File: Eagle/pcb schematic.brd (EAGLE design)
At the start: 100 x 80 mm, 17 parts

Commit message: PCB finita
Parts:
- BLUETOOTH: device SparkFun-Connectors:1X02 -> SparkFun-Connectors:1X04
- moved R5 24.3 mm to (34.3, 39.4), turned to 0 degrees
- moved R6 16.1 mm to (50.8, 40.6), turned to 0 degrees
- moved R1 16.1 mm to (27.9, 30.5), turned to 90 degrees
- moved R7 12.8 mm to (61.0, 38.1), turned to 180 degrees
- moved FLEX1 12.7 mm to (30.5, 47.0), turned to 270 degrees
- moved FLEX2 11.4 mm to (47.0, 47.0), turned to 270 degrees
- moved BLUETOOTH 10.5 mm to (41.9, 30.5), turned to 0 degrees
- moved FSR 10.2 mm to (71.1, 47.0)
- moved FLEX3 10.2 mm to (61.0, 47.0)
- moved PIN_10 8.89 mm to (41.9, 25.4)
- moved R8 7.18 mm to (74.9, 35.6)
- moved J1 6.35 mm to (19.1, 44.5), turned to 90 degrees
- moved D1 5.24 mm to (34.3, 29.2)
- moved PIN_123-124 5.08 mm to (54.6, 25.4), turned to 180 degrees
- moved PIN_26-24 3.81 mm to (74.9, 25.4)
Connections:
- net GND: now also BLUETOOTH.2
- net N$4: now also BLUETOOTH.4, PIN_123-124.1; no longer BLUETOOTH.1, PIN_123-124.2
- net N$6: now also BLUETOOTH.3, PIN_123-124.2; no longer BLUETOOTH.2, PIN_123-124.1
- net N$9: now also BLUETOOTH.1
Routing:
- net N$9: track 0.00 -> 88.4 mm
- net N$1: track 0.00 -> 47.7 mm
- net N$2: track 0.00 -> 33.0 mm
- net N$3: track 0.00 -> 26.0 mm
- net N$5: track 0.00 -> 22.1 mm
- net N$4: track 0.00 -> 10.2 mm
- net N$10: track 0.00 -> 8.83 mm
- net N$11: track 0.00 -> 8.09 mm
- net N$6: track 0.00 -> 7.18 mm
- net 5V: track 0.00 -> 5.74 mm
- added copper zone on layer 1, net GND

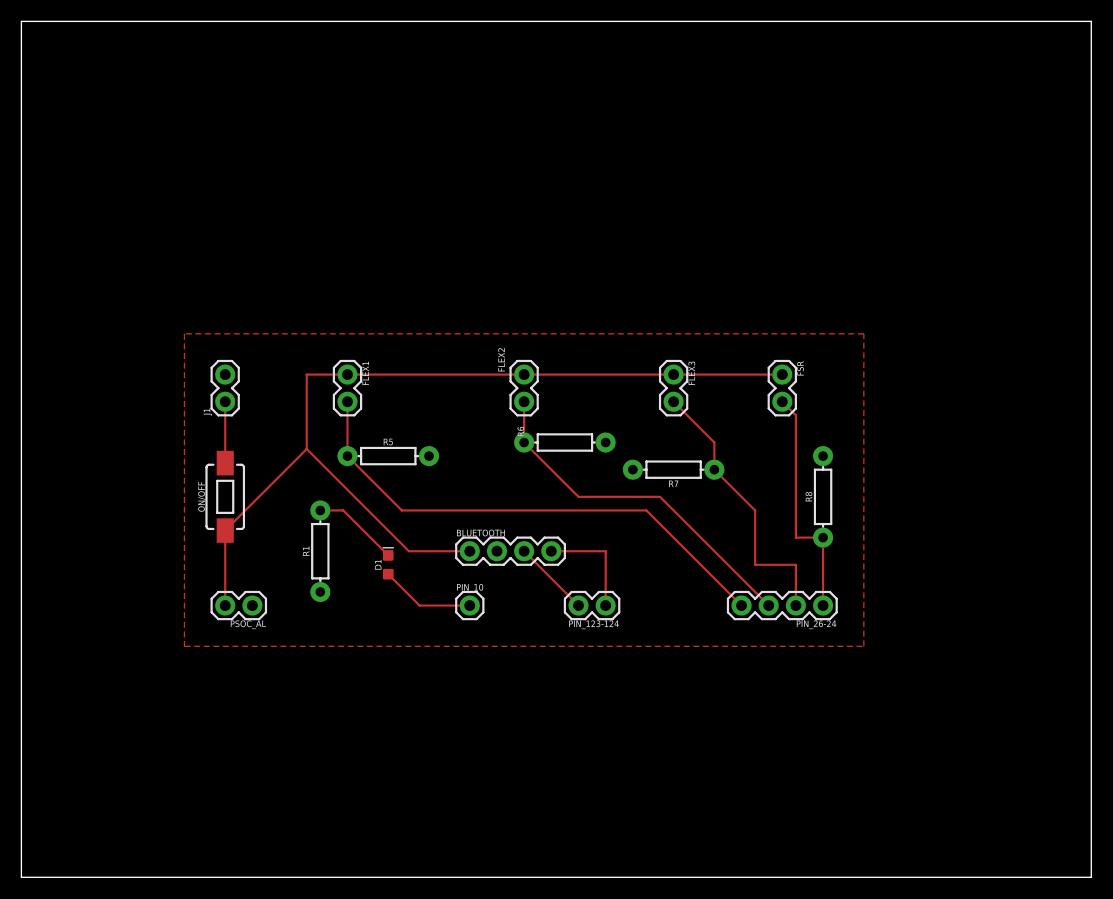
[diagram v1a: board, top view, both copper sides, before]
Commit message: PCB modifica tracce e aggiunta componenti batteria
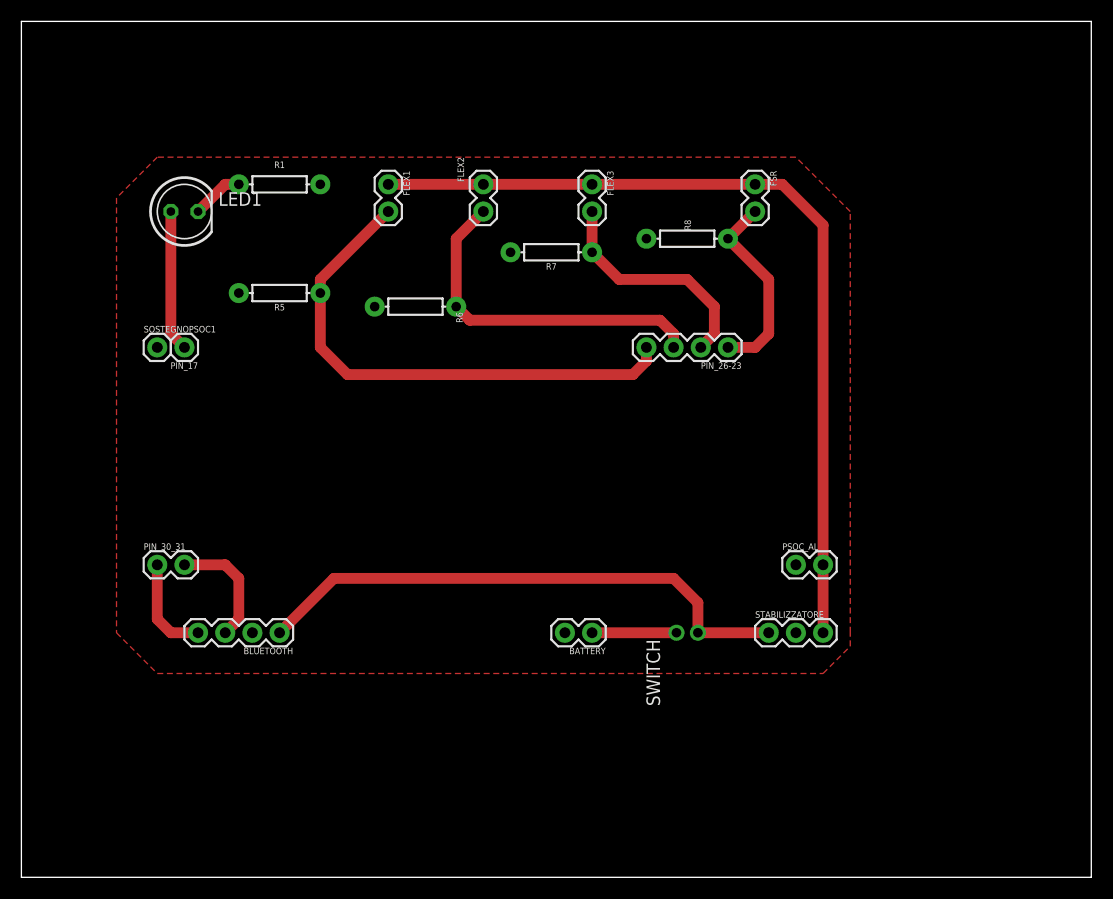
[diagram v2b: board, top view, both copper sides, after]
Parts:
- removed D1: RED, SparkFun-LED:LED-0603
- removed J1, PIN_123-124: (no value), SparkFun-Connectors:1X02
- removed ON/OFF: MOMENTARY-SWITCH-SPST-SMD-6.0X3.5MM, SparkFun-Switches:TACTILE_SWITCH_SMD_6.0X3.5MM
- removed PIN_10: (no value), SparkFun-Connectors:1X01
- removed PIN_26-24: (no value), SparkFun-Connectors:1X04
- added BATTERY, PIN_30_31: (no value), SparkFun-Connectors:1X02
- added LED1: (no value), led:LED5MM
- added PIN_17, SOSTEGNOPSOC1: (no value), SparkFun-Connectors:1X01
- added PIN_26-23: (no value), SparkFun-Connectors:1X04
- added STABILIZZATORE: 455-1750-1-ND, SparkFun-Connectors:1X03
- added SWITCH: 332-02, con-garry:332-02
- moved PSOC_AL 50.9 mm to (72.4, 29.2), turned to 0 degrees
- moved R1 34.5 mm to (24.1, 64.8), turned to 180 degrees
- moved R8 27.3 mm to (62.2, 59.7), turned to 180 degrees
- moved R7 23.3 mm to (49.5, 58.4)
- moved BLUETOOTH 19.3 mm to (24.1, 22.9), turned to 180 degrees
- moved FLEX3 19.3 mm to (53.3, 64.8)
- moved R6 18.9 mm to (36.8, 53.3), turned to 180 degrees
- moved R5 18.3 mm to (24.1, 54.6), turned to 180 degrees
- moved FLEX1 18.2 mm to (34.3, 64.8)
- moved FLEX2 18.2 mm to (43.2, 64.8)
- moved FSR 18.0 mm to (68.6, 64.8)
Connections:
- removed net N$11: D1.C, R1.P$2
- removed net N$9: BLUETOOTH.1, FLEX1.1, FLEX2.1, FLEX3.1, FSR.1, ON/OFF.1, PSOC_AL.2
- new net N$12: FLEX1.1, FLEX2.1, FLEX3.1, FSR.1, PSOC_AL.2, STABILIZZATORE.3
- new net N$7: LED1.A, PIN_17.1
- new net N$8: LED1.K, R1.P$2
- net 5V: now also BATTERY.1, SWITCH.1; no longer J1.1, ON/OFF.2
- net GND: now also BATTERY.2, STABILIZZATORE.2; no longer J1.2
- net N$1: now also PIN_26-23.4; no longer PIN_26-24.4
- net N$10: now also BLUETOOTH.1, STABILIZZATORE.1, SWITCH.2; no longer D1.A, PIN_10.1
- net N$2: now also PIN_26-23.3; no longer PIN_26-24.3
- net N$3: now also PIN_26-23.2; no longer PIN_26-24.2
- net N$4: now also BLUETOOTH.3, PIN_30_31.2; no longer BLUETOOTH.4, PIN_123-124.1
- net N$5: now also PIN_26-23.1; no longer PIN_26-24.1
- net N$6: now also BLUETOOTH.4, PIN_30_31.1; no longer BLUETOOTH.3, PIN_123-124.2
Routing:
- net N$9: track 88.4 -> 0.00 mm
- net N$12: track 0.00 -> 80.3 mm
- net N$10: track 8.83 -> 51.6 mm
- net N$7: track 0.00 -> 13.2 mm
- net N$11: track 8.09 -> 0.00 mm
- net N$8: track 0.00 -> 4.86 mm
- net N$3: track 26.0 -> 21.7 mm
- net N$5: track 22.1 -> 18.4 mm
- net N$6: track 7.18 -> 9.42 mm
- net 5V: track 5.74 -> 7.89 mm
- net N$4: track 10.2 -> 11.2 mm
- net N$1: track 47.7 -> 48.7 mm

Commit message: PCB con pin separati senza errori
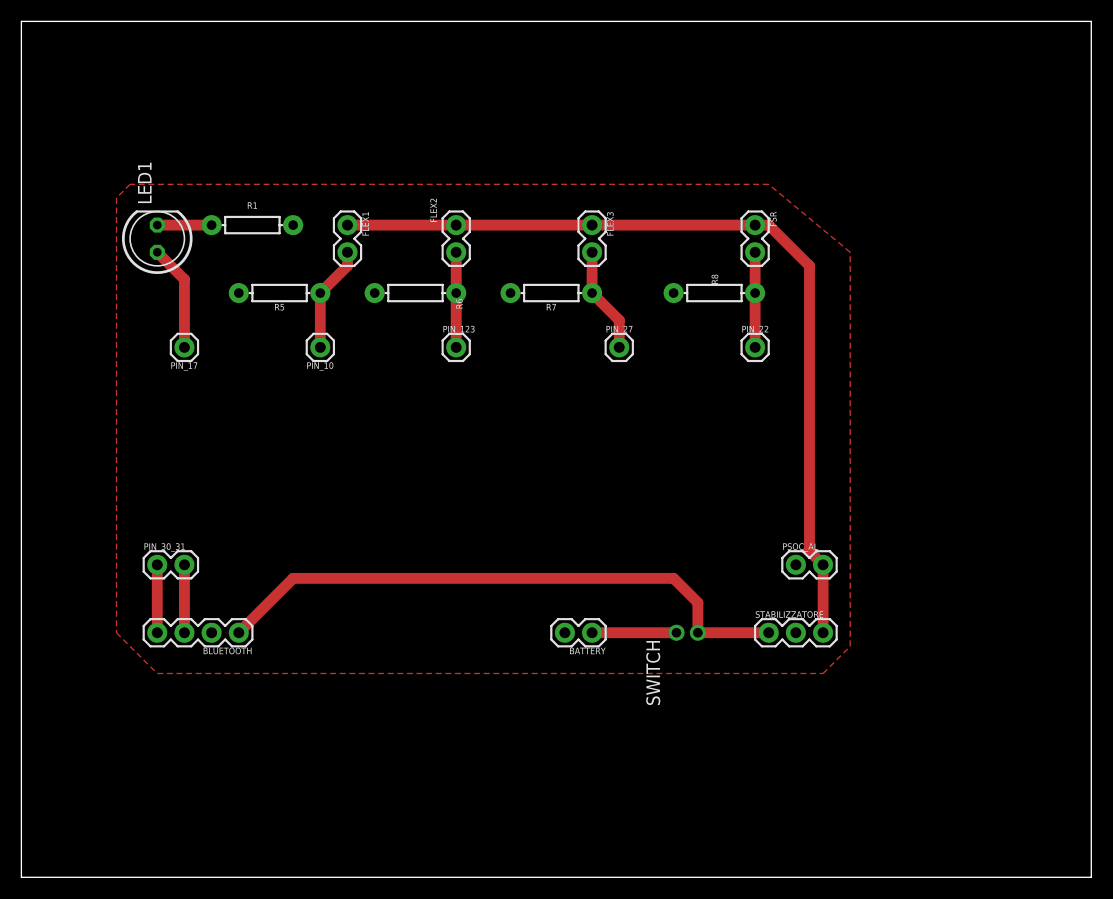
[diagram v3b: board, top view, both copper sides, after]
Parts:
- removed PIN_26-23: (no value), SparkFun-Connectors:1X04
- removed SOSTEGNOPSOC1: (no value), SparkFun-Connectors:1X01
- added PIN_10, PIN_123, PIN_22, PIN_27: (no value), SparkFun-Connectors:1X01
- moved R8 5.68 mm to (64.8, 54.6)
- moved FLEX1 5.39 mm to (30.5, 61.0)
- moved FLEX2 4.58 mm to (40.6, 61.0)
- moved R1 4.58 mm to (21.6, 61.0)
- moved R7 3.81 mm to (49.5, 54.6)
- moved BLUETOOTH 3.81 mm to (20.3, 22.9)
- moved FLEX3 3.81 mm to (53.3, 61.0)
- moved FSR 3.81 mm to (68.6, 61.0)
- moved LED1 3.59 mm to (12.7, 59.7), turned to 90 degrees
- moved R6 1.27 mm to (36.8, 54.6)
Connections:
- net N$1: now also PIN_10.1; no longer PIN_26-23.4
- net N$2: now also PIN_123.1; no longer PIN_26-23.3
- net N$3: now also PIN_27.1; no longer PIN_26-23.2
- net N$5: now also PIN_22.1; no longer PIN_26-23.1
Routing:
- net N$1: track 48.7 -> 9.94 mm
- net N$2: track 32.6 -> 8.89 mm
- net N$3: track 21.7 -> 9.94 mm
- net N$5: track 18.4 -> 8.89 mm
- net N$4: track 11.2 -> 6.35 mm
- net N$10: track 51.6 -> 55.4 mm
- net N$7: track 13.2 -> 9.94 mm
- net N$6: track 9.42 -> 6.35 mm
- net N$12: track 80.3 -> 79.6 mm

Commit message: PCB con pin separati senza errori
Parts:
- removed PIN_10, PIN_123: (no value), SparkFun-Connectors:1X01
- added PIN_12, PIN_25: (no value), SparkFun-Connectors:1X01
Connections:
- net N$1: now also PIN_12.1; no longer PIN_10.1
- net N$2: now also PIN_27.1; no longer PIN_123.1
- net N$3: now also PIN_25.1; no longer PIN_27.1
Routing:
- net N$2: track 8.89 -> 21.2 mm
- net N$3: track 9.94 -> 15.0 mm
- net N$1: track 9.94 -> 12.0 mm
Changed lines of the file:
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@@
 <attribute name="VALUE" x="68.58" y="20.828" size="0.6096" layer="27" font="vector" ratio="20"/>
 </element>
-<element name="PIN_10" library="SparkFun-Connectors" package="1X01" value="" x="27.94" y="49.53" smashed="yes" rot="R180">
-<attribute name="NAME" x="29.21" y="48.133" size="0.6096" layer="25" font="vector" ratio="20" rot="R180"/>
-<attribute name="VALUE" x="29.21" y="51.054" size="0.6096" layer="27" font="vector" ratio="20" rot="R180" align="top-left"/>
-</element>
-<element name="PIN_123" library="SparkFun-Connectors" package="1X01" value="" x="40.64" y="49.53" smashed="yes">
-<attribute name="NAME" x="39.37" y="50.927" size="0.6096" layer="25" font="vector" ratio="20"/>
-<attribute name="VALUE" x="39.37" y="48.006" size="0.6096" layer="27" font="vector" ratio="20" align="top-left"/>
+<element name="PIN_12" library="SparkFun-Connectors" package="1X01" value="" x="22.86" y="49.53" smashed="yes" rot="R180">
+<attribute name="NAME" x="24.13" y="48.133" size="0.6096" layer="25" font="vector" ratio="20" rot="R180"/>
+<attribute name="VALUE" x="24.13" y="51.054" size="0.6096" layer="27" font="vector" ratio="20" rot="R180" align="top-left"/>
 </element>
 <element name="PIN_27" library="SparkFun-Connectors" package="1X01" value="" x="55.88" y="49.53" smashed="yes">
 <attribute name="NAME" x="54.61" y="50.927" size="0.6096" layer="25" font="vector" ratio="20"/>
 <attribute name="VALUE" x="54.61" y="48.006" size="0.6096" layer="27" font="vector" ratio="20" align="top-left"/>
+</element>
+<element name="PIN_25" library="SparkFun-Connectors" package="1X01" value="" x="60.96" y="49.53" smashed="yes">
+<attribute name="NAME" x="59.69" y="50.927" size="0.6096" layer="25" font="vector" ratio="20"/>
+<attribute name="VALUE" x="59.69" y="48.006" size="0.6096" layer="27" font="vector" ratio="20" align="top-left"/>
 </element>
 <element name="PIN_22" library="SparkFun-Connectors" package="1X01" value="" x="68.58" y="49.53" smashed="yes">
@@
 <contactref element="R6" pad="P$1"/>
 <wire x1="40.64" y1="58.42" x2="40.64" y2="54.61" width="1.016" layer="1"/>
-<contactref element="PIN_123" pad="1"/>
-<wire x1="40.64" y1="54.61" x2="40.64" y2="49.53" width="1.016" layer="1"/>
+<contactref element="PIN_27" pad="1"/>
+<wire x1="55.88" y1="49.53" x2="45.72" y2="49.53" width="1.016" layer="1"/>
+<wire x1="40.64" y1="54.61" x2="45.72" y2="49.53" width="1.016" layer="1"/>
 </signal>
 <signal name="N$3">
@@
 <contactref element="R7" pad="P$1"/>
 <wire x1="53.34" y1="58.42" x2="53.34" y2="54.61" width="1.016" layer="1"/>
-<contactref element="PIN_27" pad="1"/>
-<wire x1="53.34" y1="54.61" x2="55.88" y2="52.07" width="1.016" layer="1"/>
-<wire x1="55.88" y1="52.07" x2="55.88" y2="49.53" width="1.016" layer="1"/>
+<contactref element="PIN_25" pad="1"/>
+<wire x1="53.34" y1="54.61" x2="58.42" y2="54.61" width="1.016" layer="1"/>
+<wire x1="58.42" y1="54.61" x2="60.96" y2="52.07" width="1.016" layer="1"/>
+<wire x1="60.96" y1="52.07" x2="60.96" y2="49.53" width="1.016" layer="1"/>
 </signal>
 <signal name="N$1">
@@
 <wire x1="30.48" y1="58.42" x2="30.48" y2="57.15" width="1.016" layer="1"/>
 <wire x1="30.48" y1="57.15" x2="27.94" y2="54.61" width="1.016" layer="1"/>
-<contactref element="PIN_10" pad="1"/>
-<wire x1="27.94" y1="54.61" x2="27.94" y2="49.53" width="1.016" layer="1"/>
+<contactref element="PIN_12" pad="1"/>
+<wire x1="27.94" y1="54.61" x2="22.86" y2="49.53" width="1.016" layer="1"/>
 </signal>
 <signal name="5V">

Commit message: case finito + modifica pcb
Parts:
- removed PIN_30_31: (no value), SparkFun-Connectors:1X02
- added PIN_35_36: (no value), SparkFun-Connectors:1X02
- moved BLUETOOTH 12.7 mm to (33.0, 22.9)
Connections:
- net N$4: now also PIN_35_36.2; no longer PIN_30_31.2
- net N$6: now also PIN_35_36.1; no longer PIN_30_31.1
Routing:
- net N$10: track 55.4 -> 42.7 mm
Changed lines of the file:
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@@
 <attribute name="VALUE" x="23.114" y="59.69" size="0.6096" layer="27" font="vector" ratio="20" align="top-center"/>
 </element>
-<element name="PIN_30_31" library="SparkFun-Connectors" package="1X02" value="" x="12.7" y="29.21" smashed="yes">
-<attribute name="NAME" x="11.43" y="30.607" size="0.6096" layer="25" font="vector" ratio="20"/>
-<attribute name="VALUE" x="11.43" y="27.178" size="0.6096" layer="27" font="vector" ratio="20"/>
+<element name="PIN_35_36" library="SparkFun-Connectors" package="1X02" value="" x="25.4" y="29.21" smashed="yes">
+<attribute name="NAME" x="24.13" y="30.607" size="0.6096" layer="25" font="vector" ratio="20"/>
+<attribute name="VALUE" x="24.13" y="27.178" size="0.6096" layer="27" font="vector" ratio="20"/>
 </element>
 <element name="BATTERY" library="SparkFun-Connectors" package="1X02" value="" x="53.34" y="22.86" smashed="yes" rot="R180">
@@
 <attribute name="VALUE" x="54.61" y="24.892" size="0.6096" layer="27" font="vector" ratio="20" rot="R180"/>
 </element>
-<element name="BLUETOOTH" library="SparkFun-Connectors" package="1X04" value="" x="20.32" y="22.86" smashed="yes" rot="R180">
-<attribute name="NAME" x="21.59" y="21.463" size="0.6096" layer="25" font="vector" ratio="20" rot="R180"/>
-<attribute name="PROD_ID" value="CONN-09696" x="20.32" y="22.86" size="1.778" layer="27" rot="R180" display="off"/>
-<attribute name="VALUE" x="21.59" y="24.892" size="0.6096" layer="27" font="vector" ratio="20" rot="R180"/>
+<element name="BLUETOOTH" library="SparkFun-Connectors" package="1X04" value="" x="33.02" y="22.86" smashed="yes" rot="R180">
+<attribute name="NAME" x="34.29" y="21.463" size="0.6096" layer="25" font="vector" ratio="20" rot="R180"/>
+<attribute name="PROD_ID" value="CONN-09696" x="33.02" y="22.86" size="1.778" layer="27" rot="R180" display="off"/>
+<attribute name="VALUE" x="34.29" y="24.892" size="0.6096" layer="27" font="vector" ratio="20" rot="R180"/>
 </element>
 <element name="LED1" library="led" library_urn="urn:adsk.eagle:library:259" package="LED5MM" package3d_urn="urn:adsk.eagle:package:15799/2" value="" x="12.7" y="59.69" smashed="yes" rot="R90">
@@
 <signal name="N$4">
 <contactref element="BLUETOOTH" pad="3"/>
-<contactref element="PIN_30_31" pad="2"/>
-<wire x1="15.24" y1="29.21" x2="15.24" y2="22.86" width="1.016" layer="1"/>
+<contactref element="PIN_35_36" pad="2"/>
+<wire x1="27.94" y1="22.86" x2="27.94" y2="29.21" width="1.016" layer="1"/>
 </signal>
 <signal name="N$6">
 <contactref element="BLUETOOTH" pad="4"/>
-<contactref element="PIN_30_31" pad="1"/>
-<wire x1="12.7" y1="29.21" x2="12.7" y2="22.86" width="1.016" layer="1"/>
+<contactref element="PIN_35_36" pad="1"/>
+<wire x1="25.4" y1="22.86" x2="25.4" y2="29.21" width="1.016" layer="1"/>
 </signal>
 <signal name="N$10">
@@
 <wire x1="63.23" y1="22.86" x2="63.23" y2="25.67" width="1.016" layer="1"/>
 <wire x1="63.23" y1="25.67" x2="60.96" y2="27.94" width="1.016" layer="1"/>
-<wire x1="60.96" y1="27.94" x2="25.4" y2="27.94" width="1.016" layer="1"/>
-<wire x1="25.4" y1="27.94" x2="20.32" y2="22.86" width="1.016" layer="1"/>
+<wire x1="60.96" y1="27.94" x2="38.1" y2="27.94" width="1.016" layer="1"/>
+<wire x1="38.1" y1="27.94" x2="33.02" y2="22.86" width="1.016" layer="1"/>
 </signal>
 <signal name="N$12">
